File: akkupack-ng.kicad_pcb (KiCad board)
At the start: 4 copper layers, 110 x 80 mm, 140 parts, among them J101 12V OUT, J102 36V IN, J103 36V OUT, J104 BAT, J105 OUT, J106 IN, J107 TEMP, J201 DISP, J202 SWD, J203 SPI, J204 USB serial, J301 USB serial, J401 USB serial, J501 LED SW, J502 Voltage sel, Q101 2N7002, Q201 2N7002, Q501 2N7002, Q502 BSS84, SW201 Reset, SW501 LED Enable, U101 BQ34Z100PWR-G1, U102 74HC164, U103 74HC164, U201 STM32F103CBT6, U202 USBLC6-2SC6, U203 AMS1117-3.3, U301 USBLC6-2SC6, U302 XC6206PxxxMR, U303 CH330N, U401 USBLC6-2SC6, U402 XC6206PxxxMR, U403 CH330N, Y201 8MHz, Y202 32k

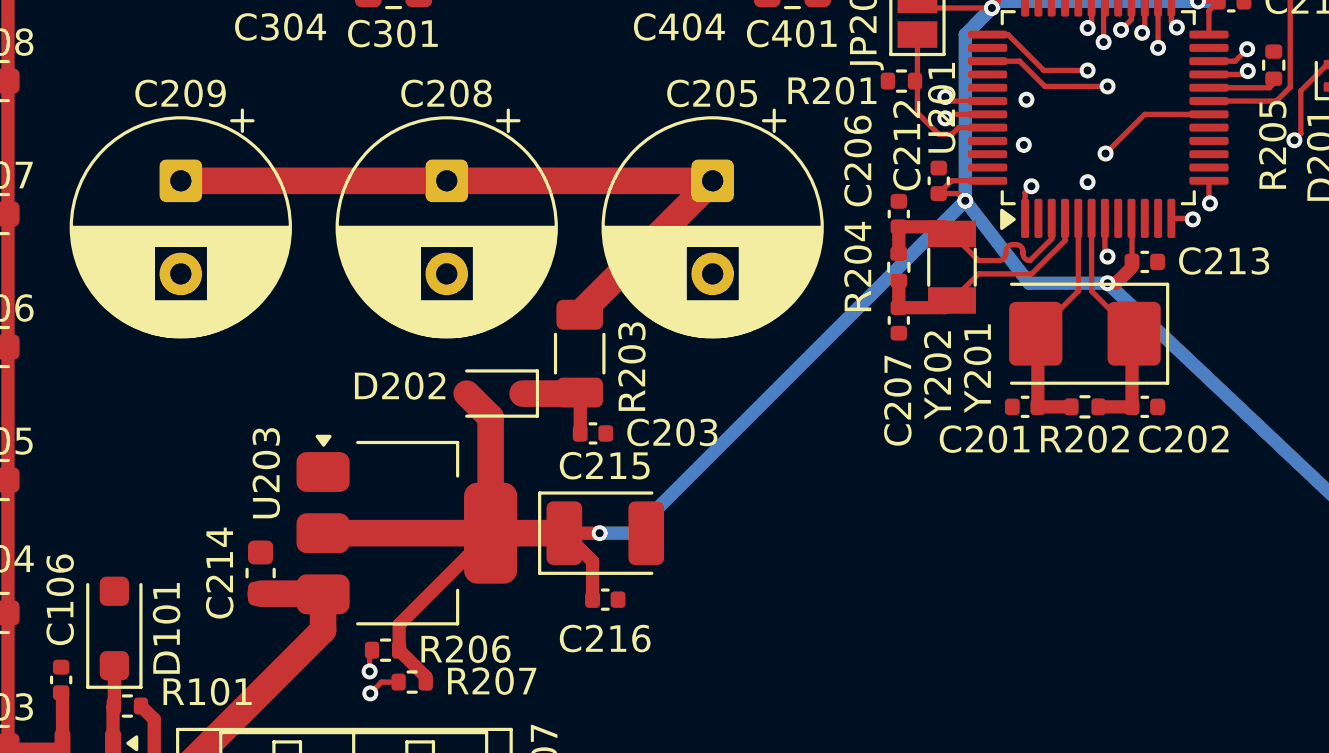
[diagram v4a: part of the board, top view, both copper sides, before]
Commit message: Add BAT power disconnector
Signed-off-by: Benedikt Spranger <b.spranger@linutronix.de>
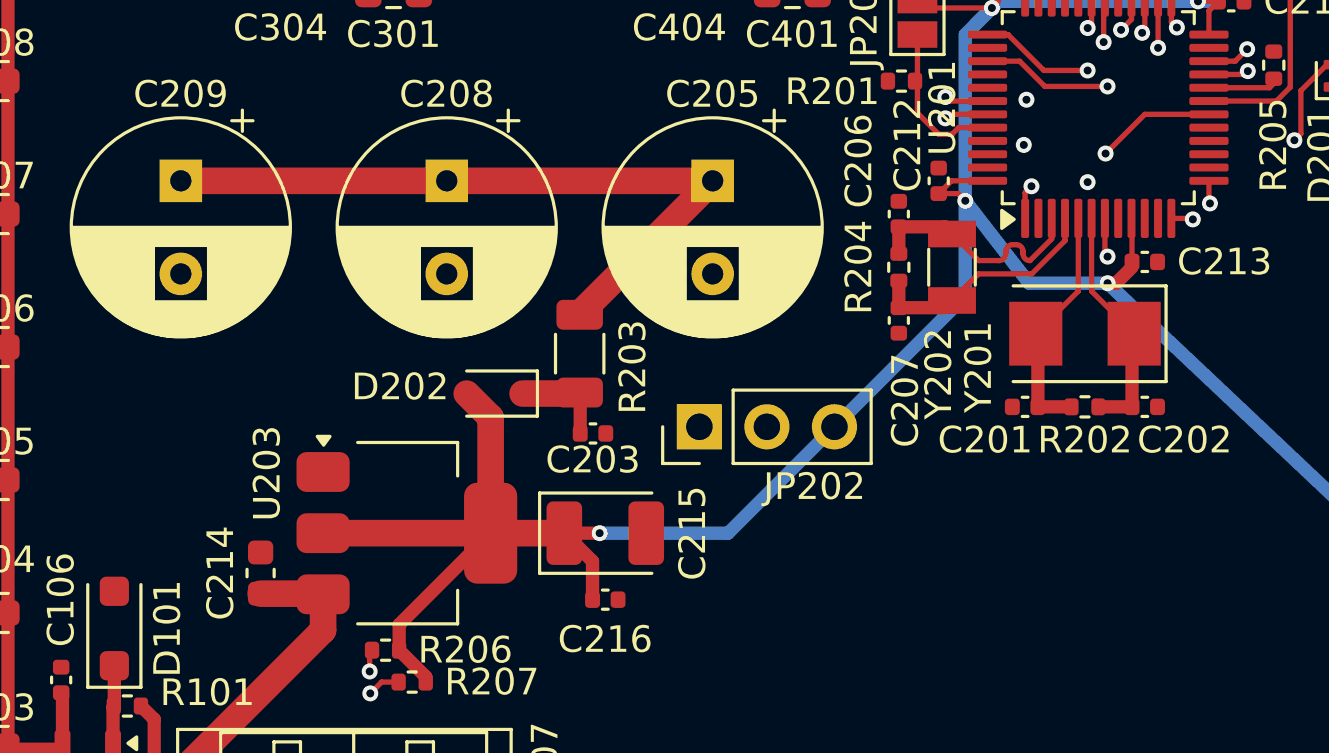
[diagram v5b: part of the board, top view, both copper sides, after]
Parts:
- added JP202: BAT Buffer, Connector_PinHeader_2.54mm:PinHeader_1x03_P2.54mm_Vertical, F.Cu at (126.0, 81.0)
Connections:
- U201 pad 1: /MCU/Vbat -> Net-(JP202-C)
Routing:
- net Net-(JP202-C): track 0.00 -> 15.0 mm, vias 0 -> 1
- net /MCU/Vbat: track 40.7 -> 37.5 mm, vias 1 -> 0
- net +3V3: track 113.6 -> 115.7 mm

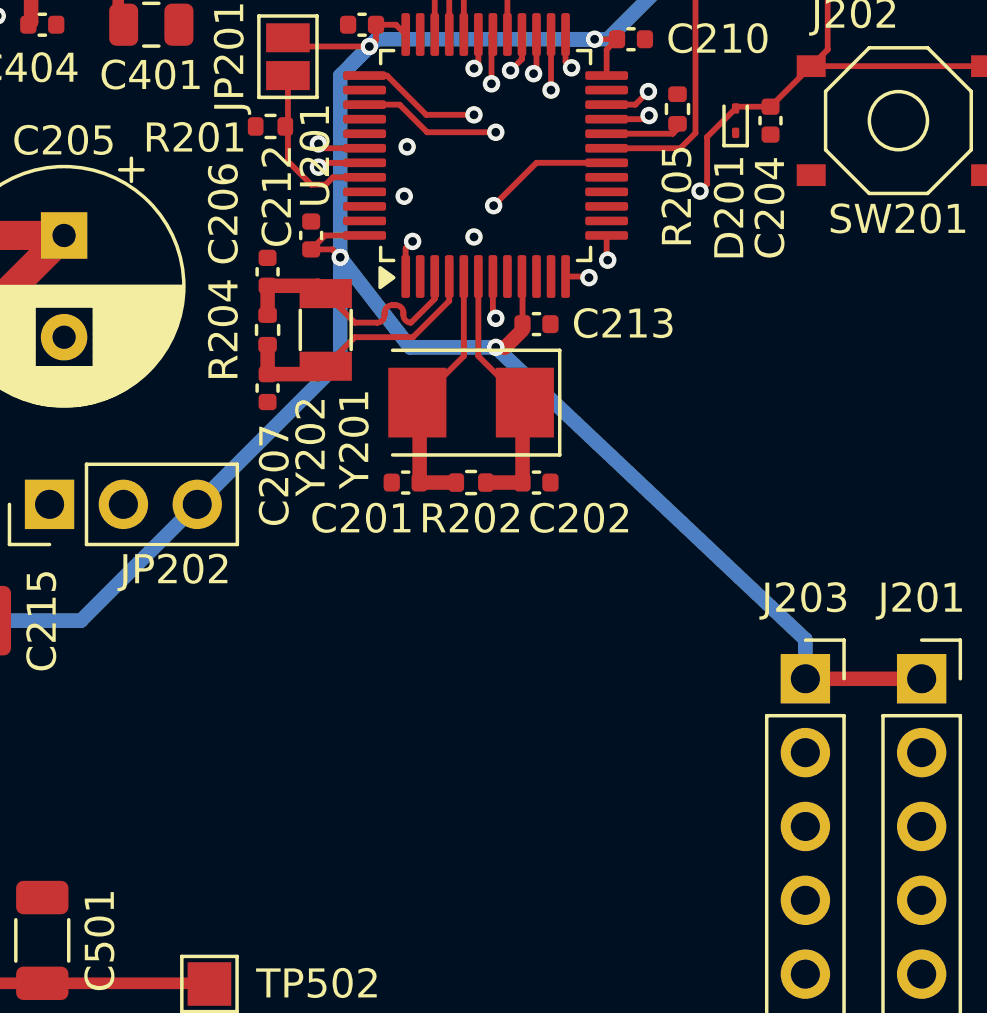
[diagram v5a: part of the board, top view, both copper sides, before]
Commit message: Add MCU LEDs
Signed-off-by: Benedikt Spranger <b.spranger@linutronix.de>
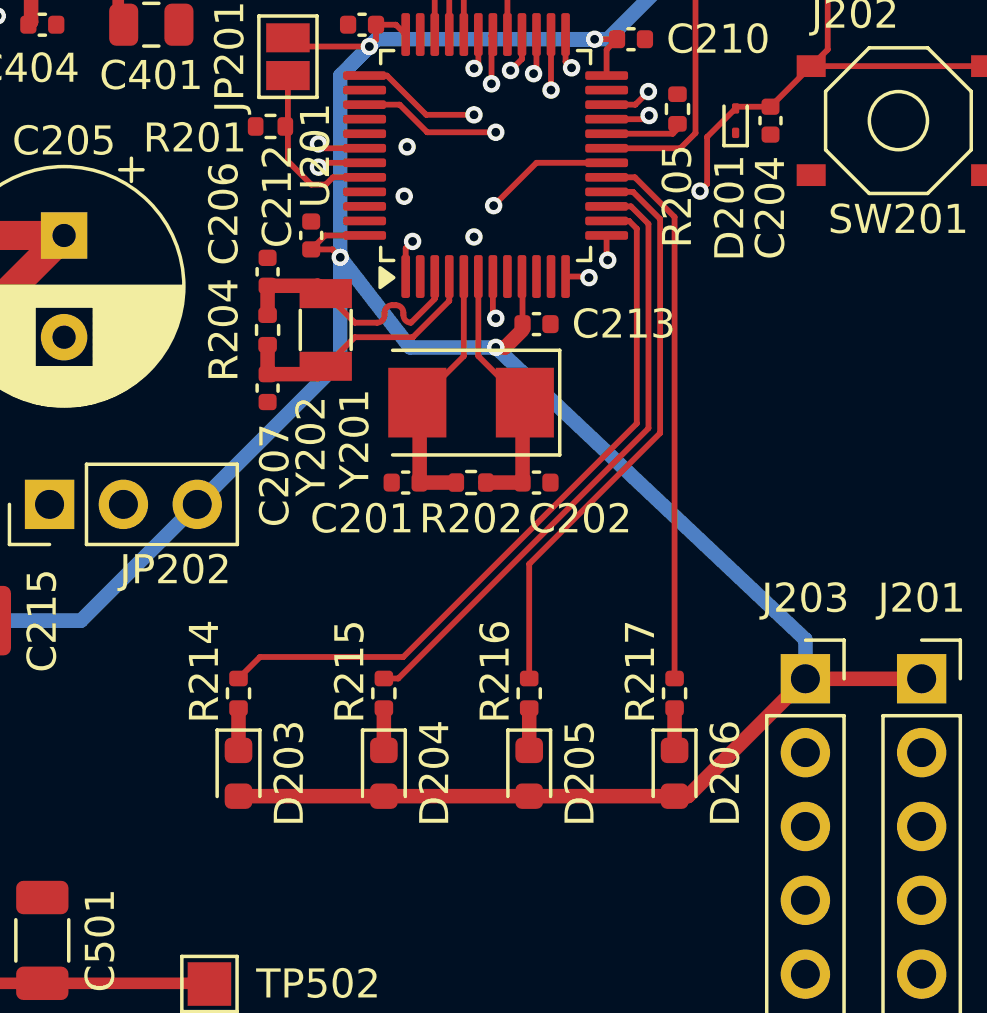
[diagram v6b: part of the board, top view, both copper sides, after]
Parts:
- added D203: RED, LED_SMD:LED_0603_1608Metric, F.Cu at (132.5, 90.2)
- added D204: RED, LED_SMD:LED_0603_1608Metric, F.Cu at (137.5, 90.2)
- added D205: RED, LED_SMD:LED_0603_1608Metric, F.Cu at (142.5, 90.2)
- added D206: RED, LED_SMD:LED_0603_1608Metric, F.Cu at (147.5, 90.2)
- added R214: 1k, Resistor_SMD:R_0402_1005Metric, F.Cu at (132.5, 87.5)
- added R215: 1k, Resistor_SMD:R_0402_1005Metric, F.Cu at (137.5, 87.5)
- added R216: 1k, Resistor_SMD:R_0402_1005Metric, F.Cu at (142.5, 87.5)
- added R217: 1k, Resistor_SMD:R_0402_1005Metric, F.Cu at (147.5, 87.5)
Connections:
- U201 pad 14: unconnected-(U201-PA4-Pad14) -> /MCU/LED1
- U201 pad 15: unconnected-(U201-PA5-Pad15) -> /MCU/LED2
- U201 pad 16: unconnected-(U201-PA6-Pad16) -> /MCU/LED3
- U201 pad 17: unconnected-(U201-PA7-Pad17) -> /MCU/LED4
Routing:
- net /MCU/LED1: track 0.00 -> 25.2 mm
- net /MCU/LED2: track 0.00 -> 21.4 mm
- net +3V3: track 115.7 -> 136.9 mm
- net /MCU/LED3: track 0.00 -> 19.9 mm
- net /MCU/LED4: track 0.00 -> 18.8 mm
- net Net-(D206-K): track 0.00 -> 1.45 mm
- net Net-(D205-K): track 0.00 -> 1.45 mm
- net Net-(D204-K): track 0.00 -> 1.45 mm
- net Net-(D203-K): track 0.00 -> 1.45 mm

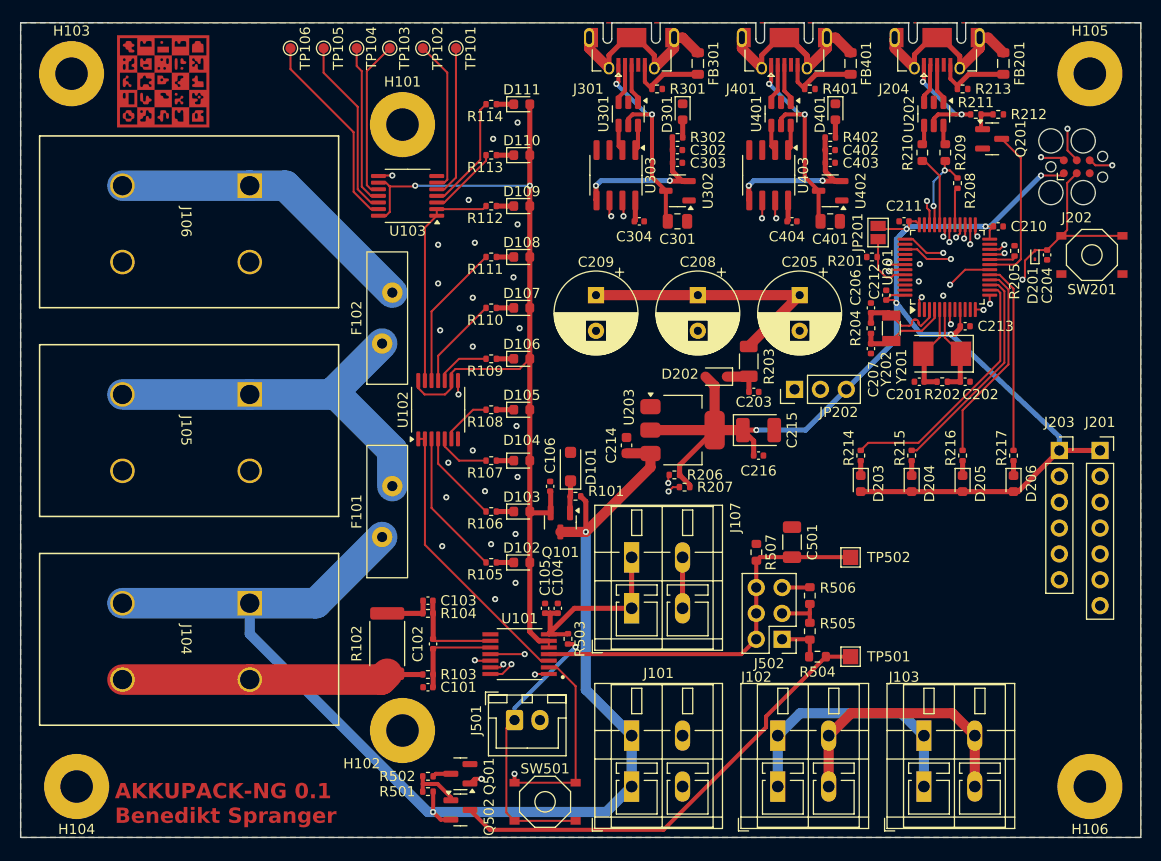
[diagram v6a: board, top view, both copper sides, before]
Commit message: Enable external I2C programming
Signed-off-by: Benedikt Spranger <b.spranger@linutronix.de>
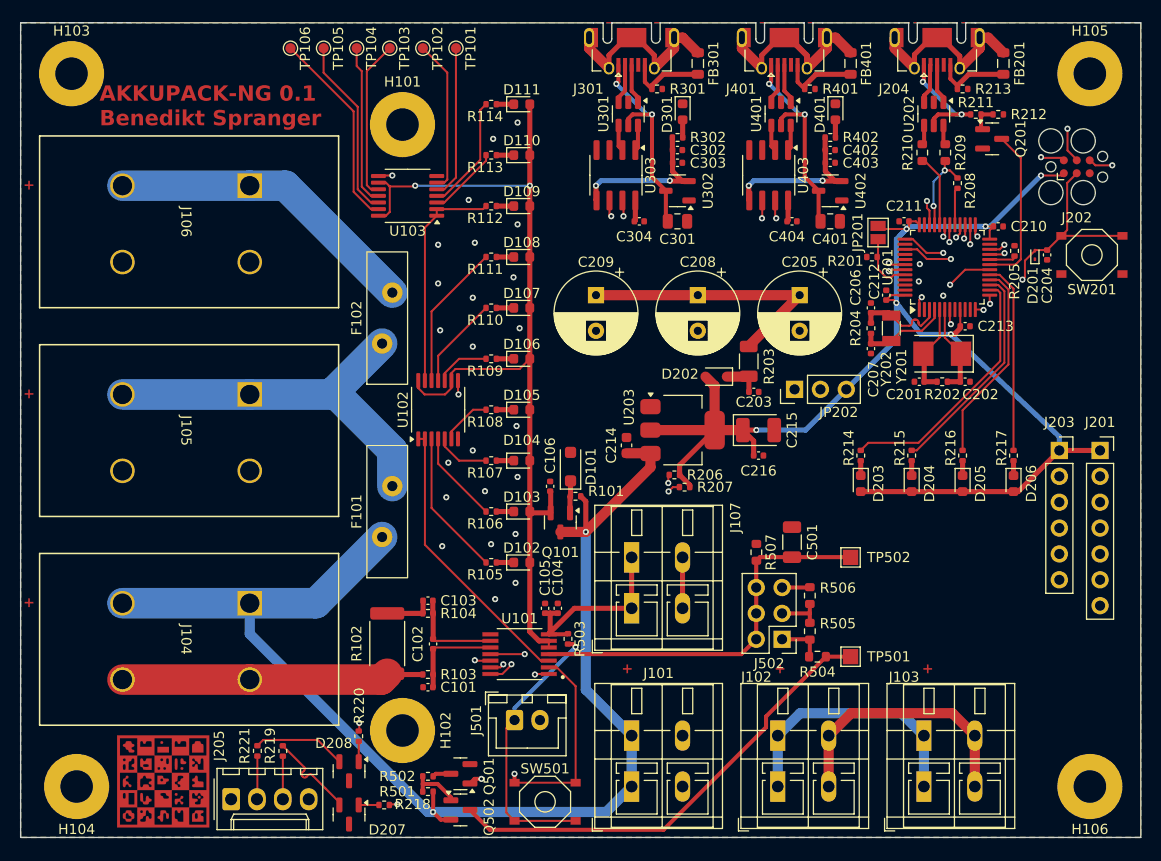
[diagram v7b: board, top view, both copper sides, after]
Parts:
- added D207: AZ23C5V6-7, Package_TO_SOT_SMD:SOT-23, F.Cu at (82.2, 122.8)
- added D208: AZ23C5V6-7, Package_TO_SOT_SMD:SOT-23, F.Cu at (82.2, 118.5)
- added J205: EXT I2C, Connector_Molex:Molex_KK-254_AE-6410-04A_1x04_P2.54mm_Vertical, F.Cu at (70.7, 121.2)
- added R218: 100, Resistor_SMD:R_0402_1005Metric, F.Cu at (85.7, 121.8)
- added R219: 100, Resistor_SMD:R_0402_1005Metric, F.Cu at (75.8, 116.5)
- added R220: 100, Resistor_SMD:R_0402_1005Metric, F.Cu at (83.2, 115.1)
- added R221: 100, Resistor_SMD:R_0402_1005Metric, F.Cu at (73.2, 116.5)
- moved G*** 68.8 mm to (64.0, 119.5)
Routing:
- net /SDA: track 59.3 -> 78.5 mm, vias 3 -> 4
- net /SCL: track 59.0 -> 78.1 mm, vias 3 -> 4
- net Net-(D207-K-Pad2): track 0.00 -> 9.18 mm
- net Net-(D208-K-Pad2): track 0.00 -> 9.17 mm
- net Net-(J205-Pin_2): track 0.00 -> 4.26 mm
- net Net-(J205-Pin_3): track 0.00 -> 4.23 mm
- net Net-(D208-K-Pad1): track 0.00 -> 1.99 mm
- net Net-(D207-K-Pad1): track 0.00 -> 1.99 mm
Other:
- board text added: "+"
